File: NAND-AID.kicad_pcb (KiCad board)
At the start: 2 copper layers, 33.7 x 21.4 mm, 20 parts

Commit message: Add logo
Signed-off-by: Thomas Rohloff <v10lator@myway.de>
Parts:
- added G***: LOGO Emoji, V10lator's footprints:LOGO Emoji, F.Cu at (146.0, 99.9)
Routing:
- net GND: track 3466.1 -> 3305.0 mm

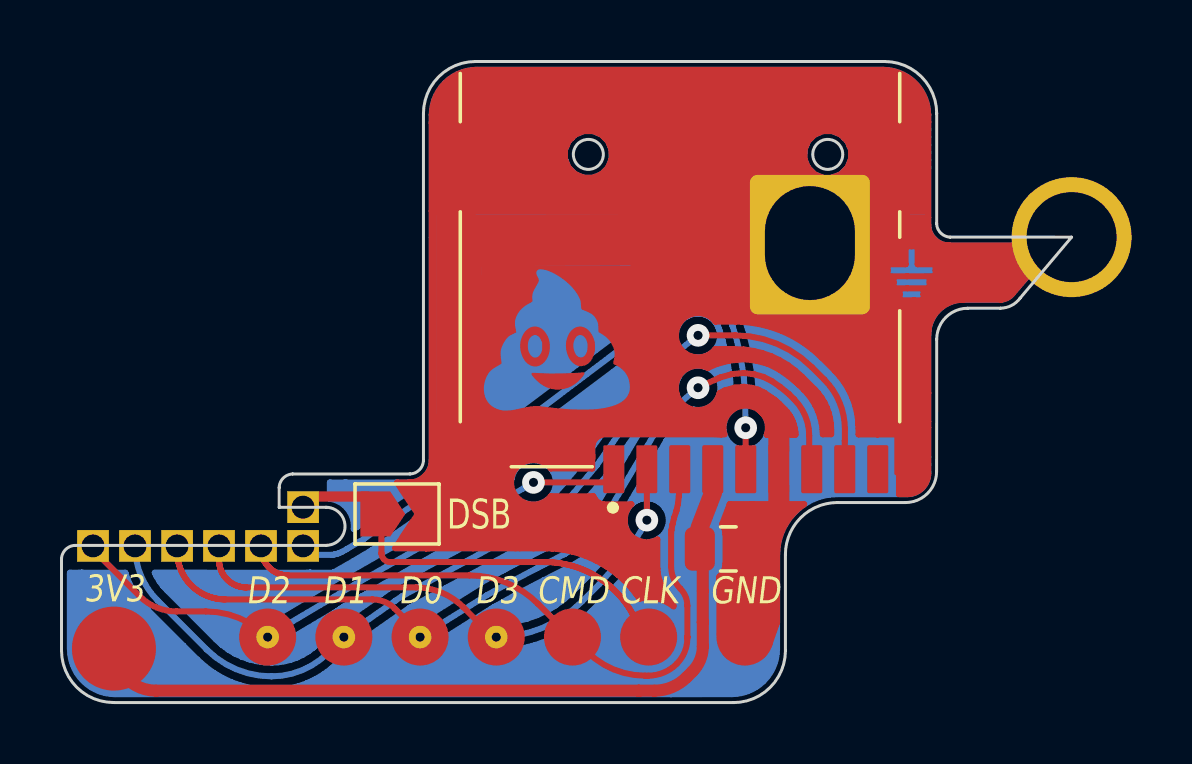
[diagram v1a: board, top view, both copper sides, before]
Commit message: Change logo
Signed-off-by: Thomas Rohloff <v10lator@myway.de>
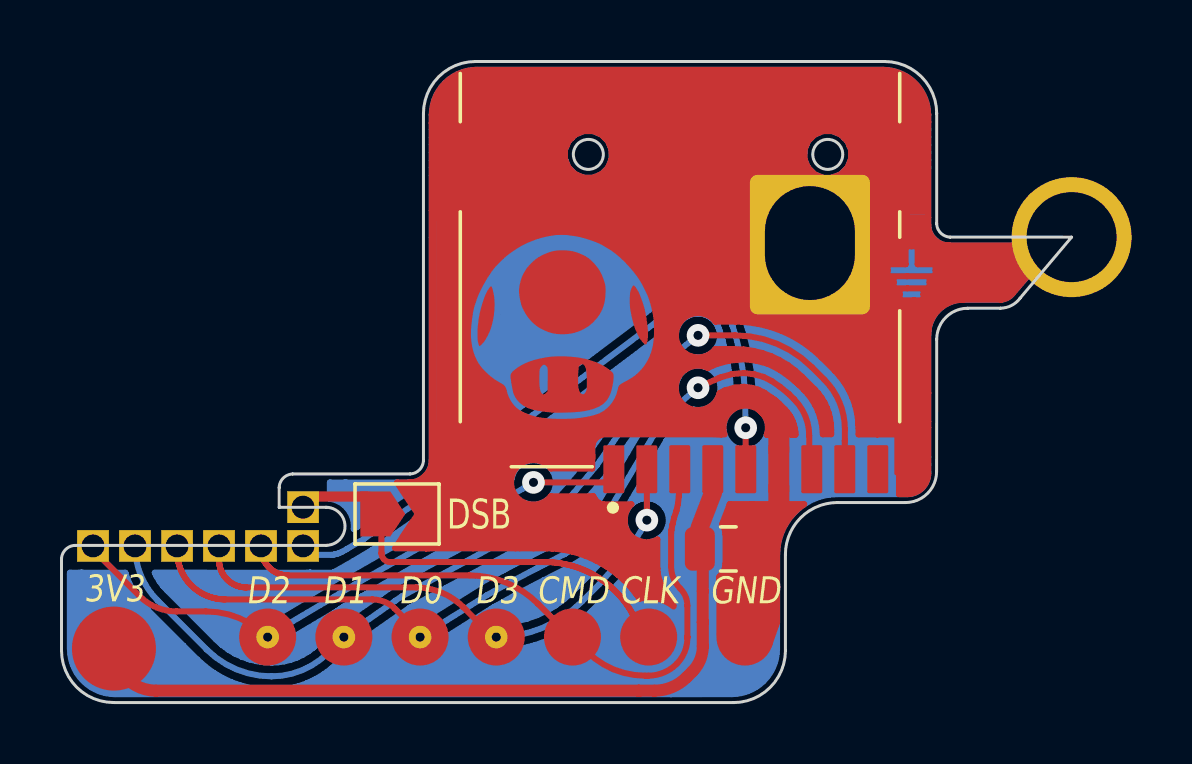
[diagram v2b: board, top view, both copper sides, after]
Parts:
- removed the G*** at (146.0, 99.9)
- added G***: LOGO Toad, V10lator's footprints:LOGO Toad, F.Cu at (146.2, 99.4)
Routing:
- net GND: track 3305.0 -> 3108.7 mm

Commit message: Remove last DRC warnings
Signed-off-by: Thomas Rohloff <v10lator@myway.de>
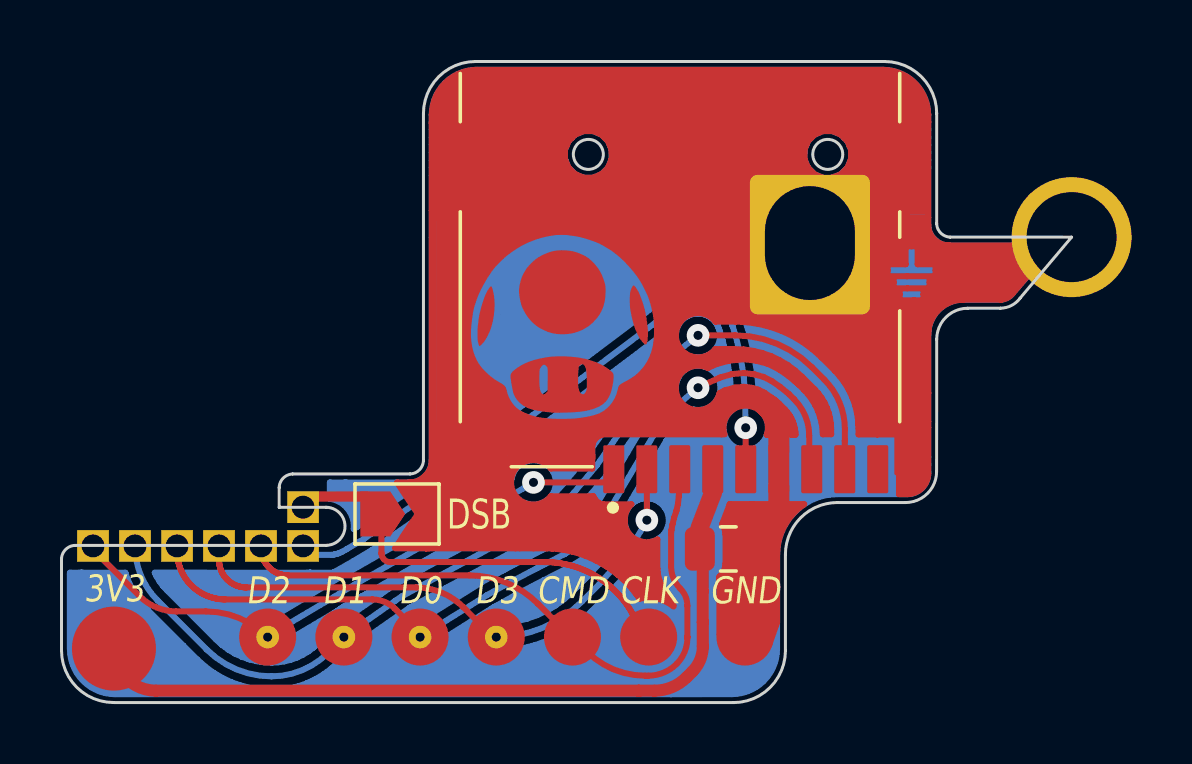
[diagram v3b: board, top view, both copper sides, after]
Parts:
- removed the ? at (154.5, 96.6)
- removed the ? at (163.2, 96.4)
- removed the DSB at (140.7, 105.6)
- added ?: , V10lator's footprints:GND hole, F.Cu at (154.5, 96.6)
- added ?: , V10lator's footprints:GND Half Hole, F.Cu at (163.2, 96.4)
- added DSB: SolderJumper-2_P1.3mm_Open_TrianglePad1.0x1.5mm EDITED SILK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, V10lator's footprints:SolderJumper-2_P1.3mm_Open_TrianglePad1.0x1.5mm EDITED SILKSCREEN, F.Cu at (140.7, 105.6)
- C1: footprint Capacitor_SMD:C_0805_2012Metric -> V10lator's footprints:C_0805_2012Metric NO SILKSCREEN
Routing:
- net GND: track 3108.7 -> 3104.1 mm
